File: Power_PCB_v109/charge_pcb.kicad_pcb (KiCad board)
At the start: 2 copper layers, 128.1 x 64 mm, 79 parts, among them J1 Mow3, J10 Mot_Left, J11 DC/DC1, J12 DC/DC2, J2 Main_PCB1, J3 Mow2, J4 Battery, J5 Main_PCB2, J6 Power Switch, J7 Mow1, J8 Mot_Right, J9 Start, Q1 BC547C, Q2 IRF9540N, Q3 BC547C, Q4 IRF9540N, U1 INA226, U2 INA226, U3 INA226, U4 INA226, U5 INA226, U6 INA226

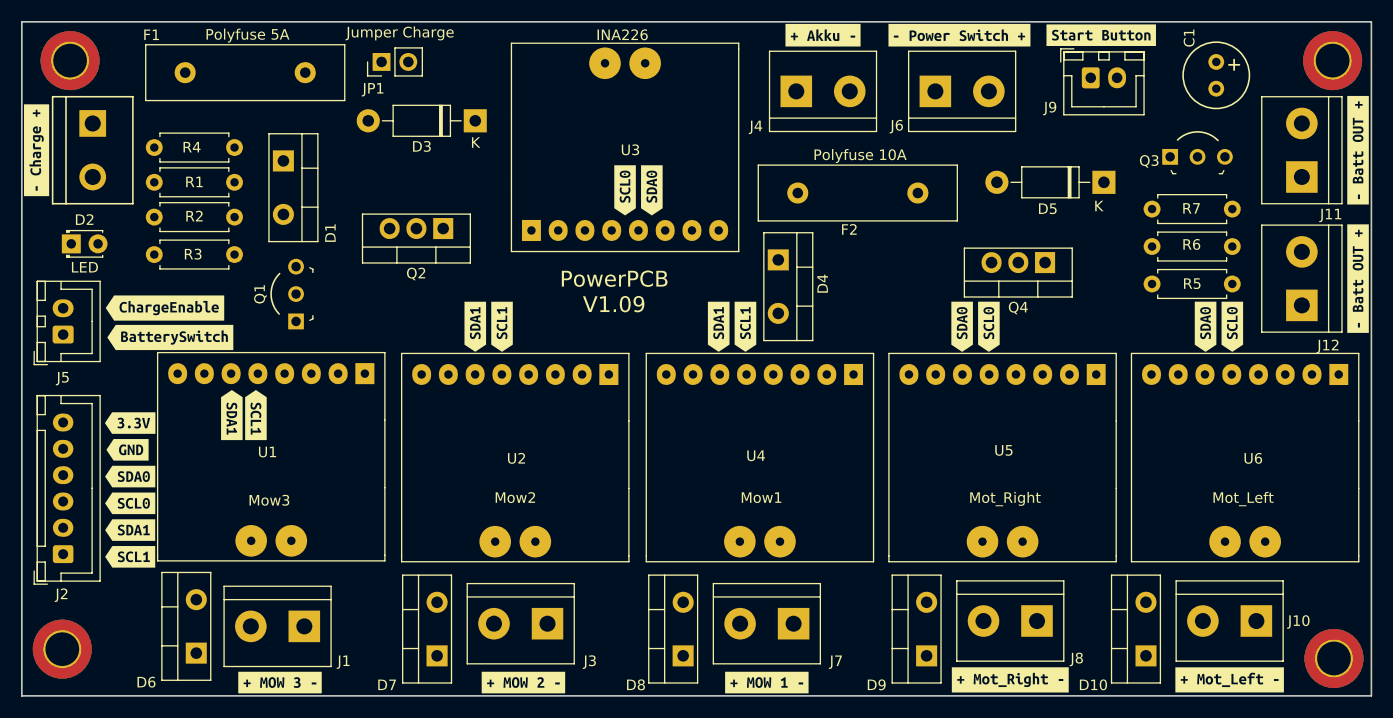
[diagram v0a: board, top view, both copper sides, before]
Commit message: Update PDF, Picture, Route
Update the PDF File of the Board.
Update PCB Picture.
Route the PCB
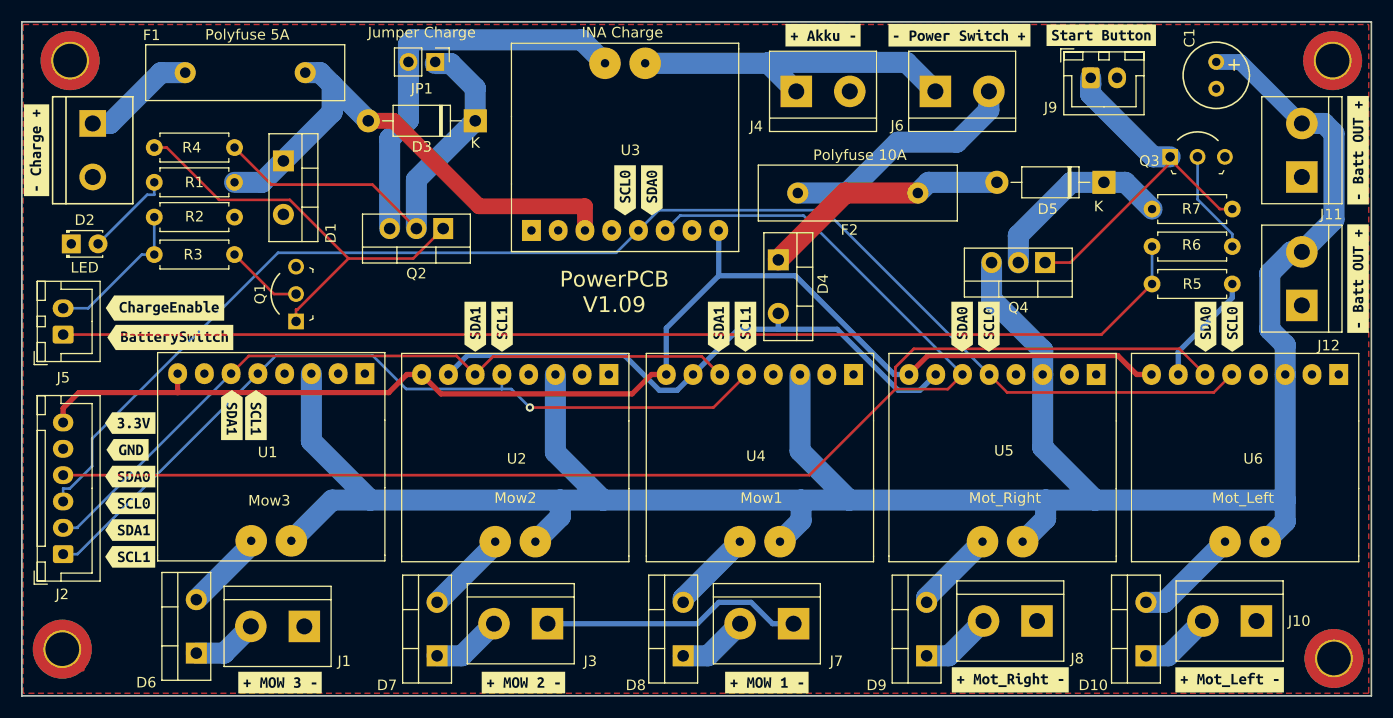
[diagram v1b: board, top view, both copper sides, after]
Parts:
- U3: value INA226 -> INA Charge
- moved JP1 5.09 mm to (124.0, 65.0), turned to -90 degrees
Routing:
- net V_Bat: track 0.00 -> 236.4 mm
- net SDA0: track 0.00 -> 157.6 mm
- net SCL0: track 0.00 -> 132.5 mm
- net +3V3: track 0.00 -> 125.5 mm
- net pinBatterySwitch: track 0.00 -> 108.9 mm
- net GND: track 0.00 -> 94.2 mm
- net SCL1: track 0.00 -> 77.4 mm, vias 0 -> 1
- net SDA1: track 0.00 -> 71.3 mm
- net V_CHARGE: track 0.00 -> 48.8 mm
- net Net-(Q1-Pad1): track 0.00 -> 41.1 mm
- net Net-(D3-Pad1): track 0.00 -> 40.9 mm
- net Net-(JP1-Pad2): track 0.00 -> 38.0 mm
- net Net-(J9-Pad1): track 0.00 -> 35.7 mm
- net Net-(J4-Pad1): track 0.00 -> 32.5 mm
- net Net-(D4-Pad1): track 0.00 -> 23.8 mm
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- added copper zone on F.Cu, net GND

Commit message: Add some Logos to PCB
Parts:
- added REF**: WEEE-Logo_5.6x8mm_SilkScreen, Symbol:WEEE-Logo_5.6x8mm_SilkScreen, B.Cu at (96.0, 110.7)
- added REF**: OSHW-Logo2_9.8x8mm_SilkScreen, Symbol:OSHW-Logo2_9.8x8mm_SilkScreen, B.Cu at (96.0, 120.4)

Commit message: Add Gerber Files
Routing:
- net GND: track 94.2 -> 69.2 mm
- net Net-(J9-Pad1): track 35.7 -> 37.7 mm
- net Net-(Q1-Pad1): track 41.1 -> 42.8 mm
- net Net-(D3-Pad1): track 40.9 -> 42.3 mm
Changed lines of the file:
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@@
       (drillshape 0)
       (scaleselection 1)
-      (outputdirectory "Gerber_PowerPCB_108/")
+      (outputdirectory "Gerber_PowerPCB_1.9/")
     )
   )
@@
   (segment (start 169.9711 96.2089) (end 171.48 94.7) (width 0.5) (layer "B.Cu") (net 1))
   (segment (start 148.44 94.7) (end 146.9356 96.2044) (width 0.5) (layer "B.Cu") (net 1))
-  (segment (start 157.988 118.364) (end 155.9837 118.364) (width 0.5) (layer "B.Cu") (net 1))
   (segment (start 156.535 88.9) (end 156.535 90.4043) (width 0.5) (layer "B.Cu") (net 1))
   (segment (start 194.51 92.5443) (end 194.51 94.7) (width 0.5) (layer "B.Cu") (net 1))
@@
   (segment (start 199.644 86.106) (end 199.644 87.4103) (width 0.5) (layer "B.Cu") (net 1))
   (segment (start 199.644 87.4103) (end 194.51 92.5443) (width 0.5) (layer "B.Cu") (net 1))
-  (segment (start 150.879 116.3371) (end 148.8521 118.364) (width 0.5) (layer "B.Cu") (net 1))
   (segment (start 156.535 90.4043) (end 152.7357 90.4043) (width 0.5) (layer "B.Cu") (net 1))
   (segment (start 167.9272 96.2089) (end 169.9711 96.2089) (width 0.5) (layer "B.Cu") (net 1))
-  (segment (start 148.8521 118.364) (end 134.62 118.364) (width 0.5) (layer "B.Cu") (net 1))
-  (segment (start 155.9837 118.364) (end 153.9568 116.3371) (width 0.5) (layer "B.Cu") (net 1))
   (segment (start 146.9356 96.2044) (end 145.242 96.2044) (width 0.5) (layer "B.Cu") (net 1))
-  (segment (start 153.9568 116.3371) (end 150.879 116.3371) (width 0.5) (layer "B.Cu") (net 1))
   (segment (start 145.242 96.2044) (end 141.9307 92.8931) (width 0.5) (layer "B.Cu") (net 1))
   (segment (start 88.629 88.412) (end 91.0007 88.412) (width 0.254) (layer "B.Cu") (net 2))
@@
   (segment (start 88.629 90.912) (end 187.218 90.912) (width 0.254) (layer "F.Cu") (net 3))
   (segment (start 192.024 82.55) (end 192.024 86.106) (width 0.254) (layer "B.Cu") (net 3))
-  (segment (start 103.4319 78.1206) (end 98.4633 73.152) (width 0.254) (layer "F.Cu") (net 4))
-  (segment (start 115.7267 83.6895) (end 115.7267 83.6894) (width 0.254) (layer "F.Cu") (net 4))
-  (segment (start 115.7267 83.6894) (end 110.8854 88.5307) (width 0.254) (layer "F.Cu") (net 4))
-  (segment (start 115.7267 83.6894) (end 110.1578 78.1206) (width 0.254) (layer "F.Cu") (net 4))
-  (segment (start 110.8854 88.5307) (end 110.744 88.5307) (width 0.254) (layer "F.Cu") (net 4))
-  (segment (start 110.744 89.662) (end 110.744 88.5307) (width 0.254) (layer "F.Cu") (net 4))
-  (segment (start 110.1578 78.1206) (end 103.4319 78.1206) (width 0.254) (layer "F.Cu") (net 4))
-  (segment (start 97.282 73.152) (end 98.4633 73.152) (width 0.254) (layer "F.Cu") (net 4))
-  (segment (start 124.714 80.843) (end 121.8675 83.6895) (width 0.254) (layer "F.Cu") (net 4))
-  (segment (start 121.8675 83.6895) (end 115.7267 83.6895) (width 0.254) (layer "F.Cu") (net 4))
+  (segment (start 102.848489 84.175969) (end 108.204 89.53148) (width 2) (layer "F.Cu") (net 4))
+  (segment (start 108.204 89.53148) (end 119.02552 89.53148) (width 2) (layer "F.Cu") (net 4))
+  (segment (start 97.282 73.152) (end 102.848489 78.718489) (width 2) (layer "F.Cu") (net 4))
+  (segment (start 102.848489 78.718489) (end 102.848489 84.175969) (width 2) (layer "F.Cu") (net 4))
+  (segment (start 124.714 83.843) (end 124.714 80.843) (width 2) (layer "F.Cu") (net 4))
+  (segment (start 119.02552 89.53148) (end 124.714 83.843) (width 2) (layer "F.Cu") (net 4))
   (segment (start 108.652 87.062) (end 110.744 87.062) (width 0.254) (layer "F.Cu") (net 5))
   (segment (start 104.902 83.312) (end 108.652 87.062) (width 0.254) (layer "F.Cu") (net 5))
@@
   (segment (start 150.876 81.026) (end 150.876 85.3244) (width 0.5) (layer "B.Cu") (net 7))
   (segment (start 145.9 90.3004) (end 150.876 85.3244) (width 0.5) (layer "B.Cu") (net 7))
-  (segment (start 176.784 87.5437) (end 176.784 84.074) (width 2) (layer "B.Cu") (net 8))
   (segment (start 181.918 108.392) (end 181.918 106.626) (width 2) (layer "B.Cu") (net 8))
   (segment (start 209.297511 80.008489) (end 209.297511 71.794191) (width 2) (layer "B.Cu") (net 8))
   (segment (start 206.248 83.058) (end 209.297511 80.008489) (width 2) (layer "B.Cu") (net 8))
+  (segment (start 176.77448 86.60448) (end 176.77448 84.074) (width 2) (layer "B.Cu") (net 8))
   (segment (start 135.836 108.204) (end 135.836 106.626) (width 2) (layer "B.Cu") (net 8))
   (segment (start 204.67 94.7) (end 204.67 106.626) (width 2) (layer "B.Cu") (net 8))
@@
   (segment (start 112.2 101.024) (end 117.802 106.626) (width 2) (layer "B.Cu") (net 8))
   (segment (start 181.918 106.626) (end 163.268 106.626) (width 2) (layer "B.Cu") (net 8))
+  (segment (start 176.784 87.5437) (end 176.784 86.614) (width 2) (layer "B.Cu") (net 8))
   (segment (start 186.636 106.626) (end 181.918 106.626) (width 2) (layer "B.Cu") (net 8))
   (segment (start 181.64 101.63) (end 186.636 106.626) (width 2) (layer "B.Cu") (net 8))
@@
   (segment (start 114.164 106.626) (end 110.295 110.495) (width 2) (layer "B.Cu") (net 8))
   (segment (start 181.64 94.7) (end 181.64 92.3997) (width 2) (layer "B.Cu") (net 8))
+  (segment (start 200.406 65.024) (end 198.12 65.024) (width 1.5) (layer "B.Cu") (net 8))
   (segment (start 203.198489 90.428489) (end 203.198489 85.091511) (width 2) (layer "B.Cu") (net 8))
   (segment (start 204.67 91.9) (end 203.198489 90.428489) (width 2) (layer "B.Cu") (net 8))
   (segment (start 204.67 94.7) (end 204.67 91.9) (width 2) (layer "B.Cu") (net 8))
-  (segment (start 198.12 65.024) (end 200.406 65.024) (width 1.5) (layer "B.Cu") (net 8))
   (segment (start 204.67 106.626) (end 204.67 108.67) (width 2) (layer "B.Cu") (net 8))
   (segment (start 112.2 94.62) (end 112.2 101.024) (width 2) (layer "B.Cu") (net 8))
@@
   (segment (start 204.67 108.67) (end 202.765 110.575) (width 2) (layer "B.Cu") (net 8))
   (segment (start 117.802 106.626) (end 114.164 106.626) (width 2) (layer "B.Cu") (net 8))
+  (segment (start 176.784 86.614) (end 176.77448 86.60448) (width 2) (layer "B.Cu") (net 8))
   (segment (start 205.232 83.058) (end 206.248 83.058) (width 2) (layer "B.Cu") (net 8))
   (segment (start 200.406 65.024) (end 206.248 70.866) (width 1.5) (layer "B.Cu") (net 8))
@@
   (segment (start 91.44 70.866) (end 93.0913 70.866) (width 2) (layer "B.Cu") (net 28))
   (segment (start 100.218 66.04) (end 97.9173 66.04) (width 2) (layer "B.Cu") (net 28))
-  (segment (start 96.6037 77.6353) (end 97.282 77.6353) (width 0.254) (layer "B.Cu") (net 29))
-  (segment (start 91.943 82.296) (end 96.6037 77.6353) (width 0.254) (layer "B.Cu") (net 29))
-  (segment (start 97.282 76.454) (end 97.282 77.6353) (width 0.254) (layer "B.Cu") (net 29))
-  (segment (start 194.0693 74.6006) (end 193.742 74.6006) (width 0.254) (layer "F.Cu") (net 30))
-  (segment (start 199.644 78.994) (end 198.4627 78.994) (width 0.254) (layer "F.Cu") (net 30))
-  (segment (start 193.742 74.035) (end 193.742 74.6006) (width 0.254) (layer "F.Cu") (net 30))
-  (segment (start 193.742 74.6006) (end 184.2686 84.074) (width 0.254) (layer "F.Cu") (net 30))
-  (segment (start 184.2686 84.074) (end 181.864 84.074) (width 0.254) (layer "F.Cu") (net 30))
-  (segment (start 198.4627 78.994) (end 194.0693 74.6006) (width 0.254) (layer "F.Cu") (net 30))
+  (segment (start 97.282 76.454) (end 91.943 81.793) (width 2) (layer "B.Cu") (net 29))
+  (segment (start 91.943 81.793) (end 91.943 82.296) (width 2) (layer "B.Cu") (net 29))
+  (segment (start 193.742 76.785) (end 193.742 74.035) (width 2) (layer "F.Cu") (net 30))
+  (segment (start 189.805511 78.807511) (end 189.805511 77.971489) (width 2) (layer "F.Cu") (net 30))
+  (segment (start 195.951 78.994) (end 193.742 76.785) (width 2) (layer "F.Cu") (net 30))
+  (segment (start 199.644 78.994) (end 195.951 78.994) (width 2) (layer "F.Cu") (net 30))
+  (segment (start 189.805511 77.971489) (end 193.742 74.035) (width 2) (layer "F.Cu") (net 30))
+  (segment (start 184.539022 84.074) (end 189.805511 78.807511) (width 2) (layer "F.Cu") (net 30))
+  (segment (start 181.864 84.074) (end 184.539022 84.074) (width 2) (layer "F.Cu") (net 30))
   (segment (start 186.202 67.155826) (end 186.182 67.175826) (width 2) (layer "B.Cu") (net 30))
   (segment (start 186.182 67.175826) (end 186.182 68.072) (width 2) (layer "B.Cu") (net 30))
@@
   (segment (start 152.908 118.364) (end 149.86 121.412) (width 2) (layer "B.Cu") (net 40))
   (segment (start 147.503 121.412) (end 149.86 121.412) (width 2) (layer "B.Cu") (net 40))
-  (segment (start 108.426 76.676) (end 104.902 73.152) (width 0.254) (layer "F.Cu") (net 41))
-  (segment (start 118.007 76.676) (end 108.426 76.676) (width 0.254) (layer "F.Cu") (net 41))
-  (segment (start 122.174 80.843) (end 118.007 76.676) (width 0.254) (layer "F.Cu") (net 41))
+  (segment (start 122.174 80.215717) (end 122.174 80.843) (width 2) (layer "F.Cu") (net 41))
+  (segment (start 106.181511 71.872489) (end 113.830772 71.872489) (width 2) (layer "F.Cu") (net 41))
+  (segment (start 113.830772 71.872489) (end 122.174 80.215717) (width 2) (layer "F.Cu") (net 41))
+  (segment (start 104.902 73.152) (end 106.181511 71.872489) (width 2) (layer "F.Cu") (net 41))
   (segment (start 127.762 70.612) (end 127.762 67.512) (width 2) (layer "B.Cu") (net 41))
   (segment (start 122.174 76.2) (end 122.174 80.843) (width 2) (layer "B.Cu") (net 41))

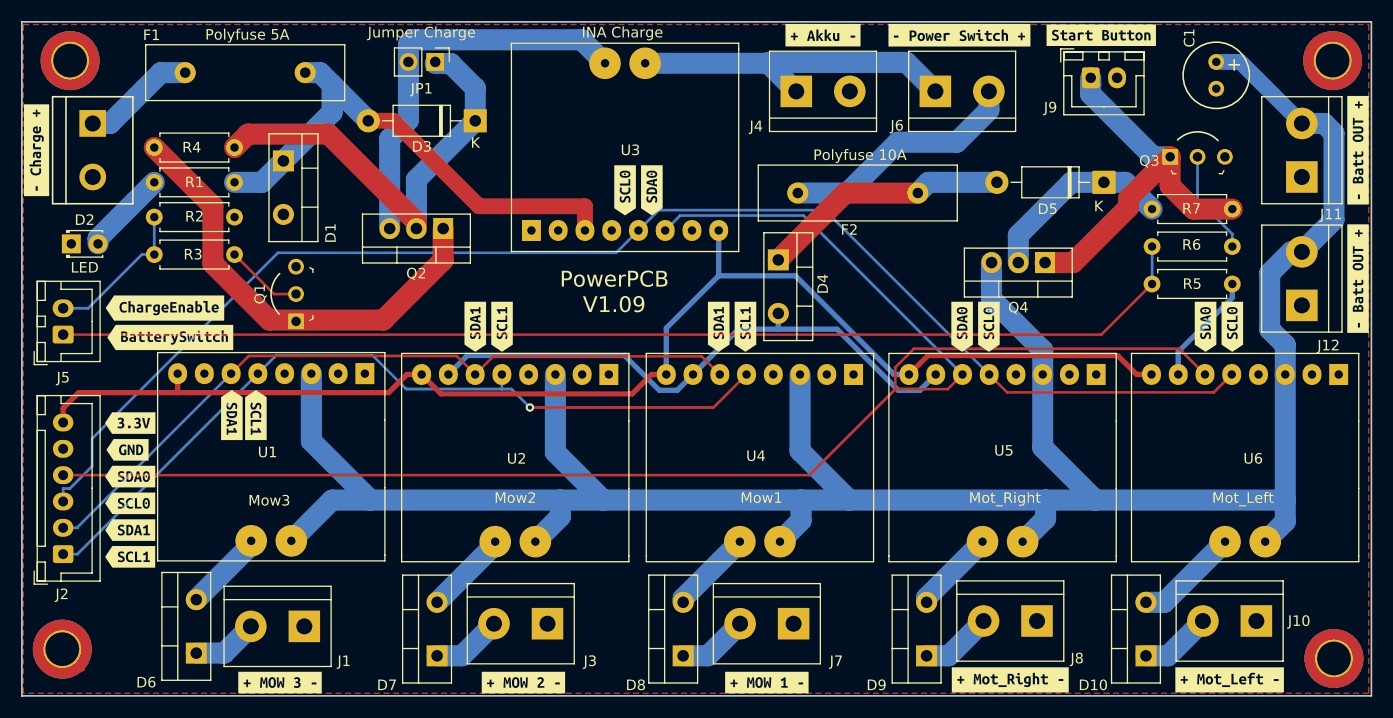
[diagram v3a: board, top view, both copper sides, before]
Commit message: Wrong Direktion of Q2 and Q4
The Drain and Source Pin was in the wrong direction.
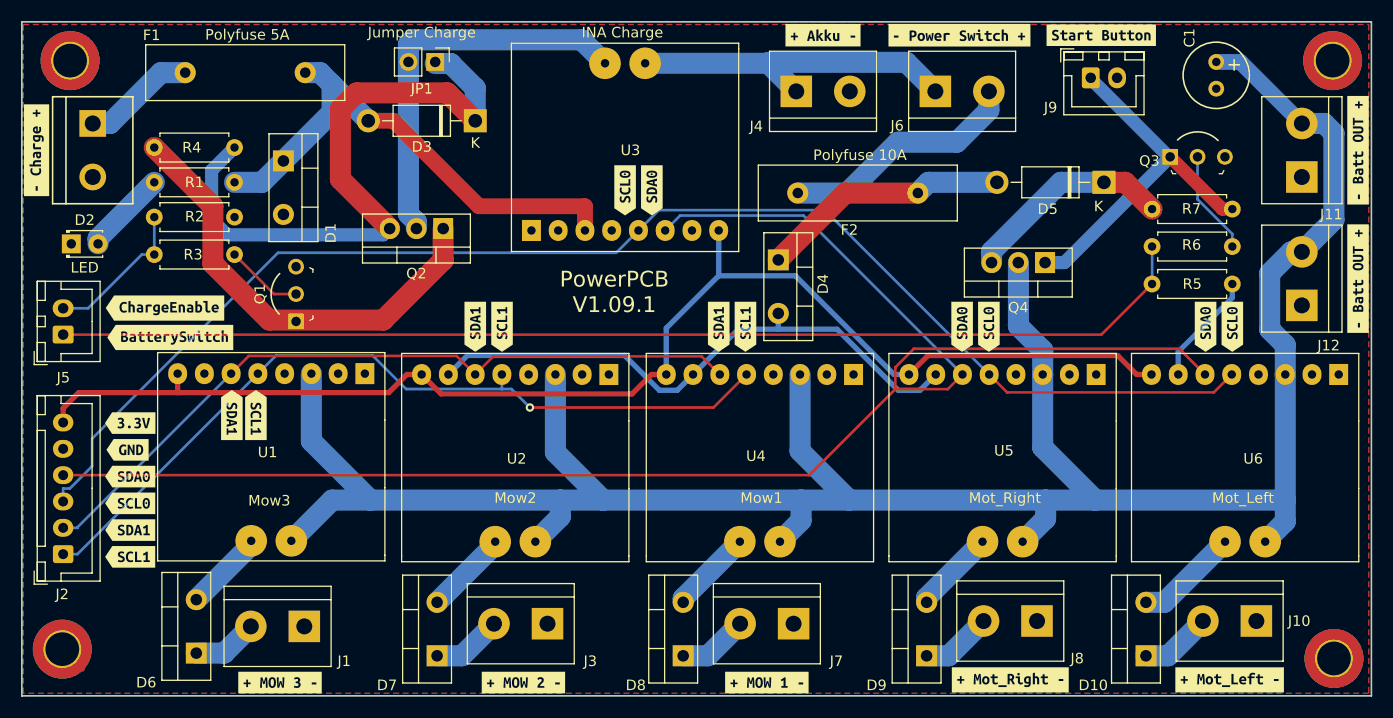
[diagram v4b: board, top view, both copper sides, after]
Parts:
- removed REF**: WEEE-Logo_5.6x8mm_SilkScreen, Symbol:WEEE-Logo_5.6x8mm_SilkScreen
- removed REF**: OSHW-Logo2_9.8x8mm_SilkScreen, Symbol:OSHW-Logo2_9.8x8mm_SilkScreen
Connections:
- Q2 pad 2: Net-(D3-Pad1) -> Net-(JP1-Pad2)
- Q2 pad 3: Net-(JP1-Pad2) -> Net-(D3-Pad1)
- Q4 pad 2: Net-(D5-Pad1) -> V_Bat
- Q4 pad 3: V_Bat -> Net-(D5-Pad1)
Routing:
- net Net-(D3-Pad1): track 42.3 -> 61.2 mm
- net Net-(J9-Pad1): track 37.7 -> 35.0 mm
- net Net-(D5-Pad1): track 18.4 -> 20.1 mm
- net V_Bat: track 236.4 -> 235.4 mm
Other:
- board text added: "PowerPCB V1.09.1"
- board text removed: "PowerPCB V1.09"
